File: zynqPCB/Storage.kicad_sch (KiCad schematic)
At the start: 22 parts, among them J3 Micro_SD_Card_Det, U16 FTDITypeUART, U17 ABRACON-ASDMB, U18 S25FL256SAGNFI001, U20F1 xc7z020clg484

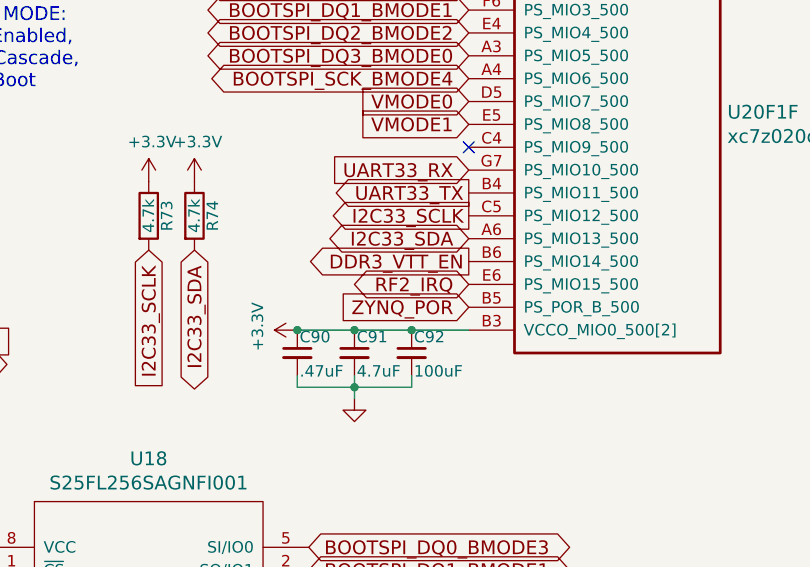
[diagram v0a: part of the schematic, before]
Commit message: Sensores Removed
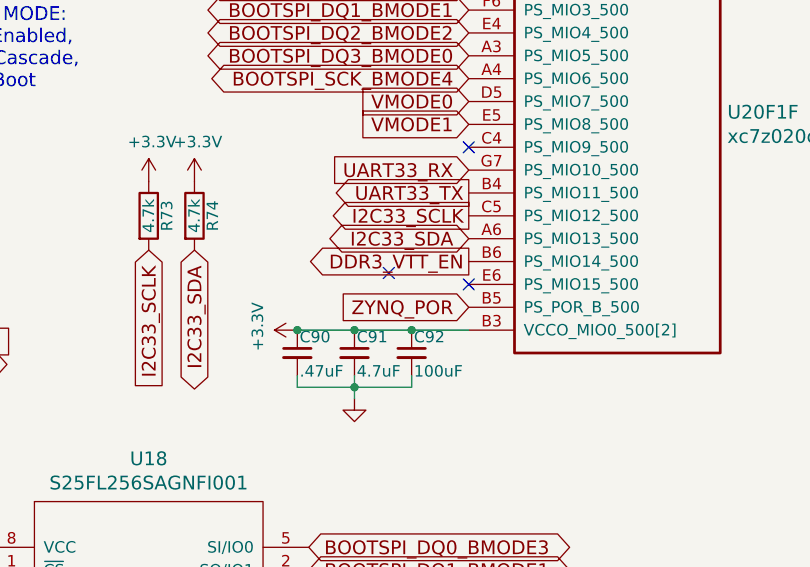
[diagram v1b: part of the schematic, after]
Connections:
- net RF2_IRQ: no longer names the net of U20F1.E6 (PS_MIO15_500)
- no-connect marks 4 -> 6
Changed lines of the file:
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@@
+	)
+	(no_connect
+		(at 198.12 101.6)
 	)
 	(no_connect
@@
 	(no_connect
 		(at 140.97 114.3)
+	)
+	(no_connect
+		(at 207.01 102.87)
 	)
 	(wire
@@
 			(effects
 				(font
-					(size 1.27 1.27)
-				)
-				(hide yes)
-			)
-		)
-	)
-	(global_label "RF2_IRQ"
-		(shape bidirectional)
-		(at 207.01 102.87 180)
-		(effects
-			(font
-				(size 1.524 1.524)
-			)
-			(justify right)
-		)
-		(property "Intersheetrefs" "${INTERSHEET_REFS}"
-			(at 207.01 102.87 0)
-			(effects
-				(font

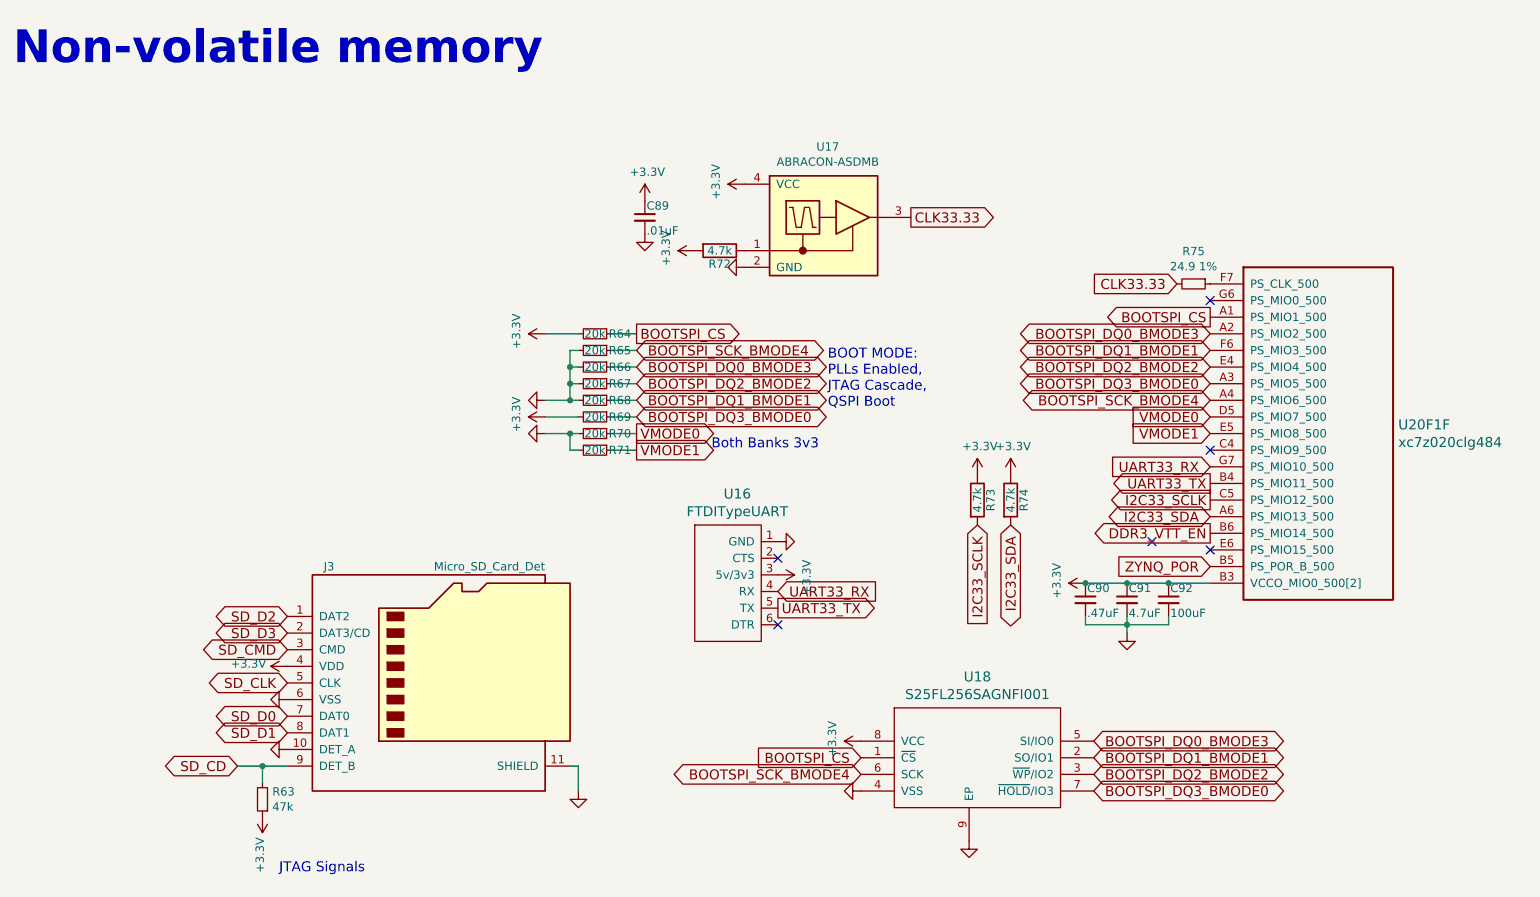
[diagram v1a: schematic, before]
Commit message: sensor changed
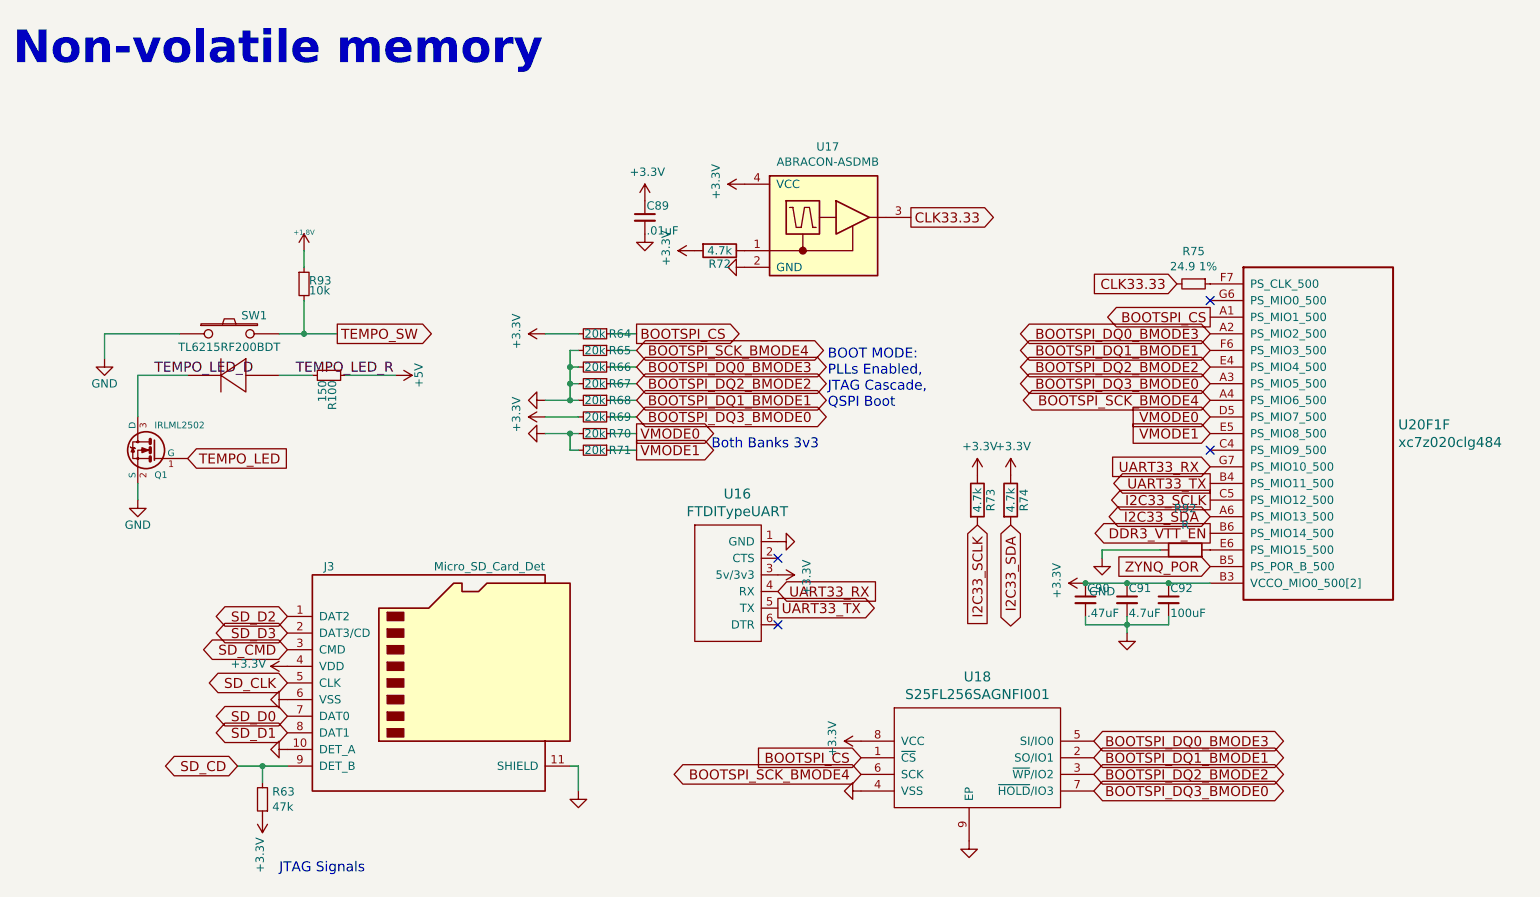
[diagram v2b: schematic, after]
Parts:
- added Q1: IRLML2502, Package_TO_SOT_SMD:SOT-23, symbol DFTBoard-rescue:IRLML2502-
- added R100: 150, Resistor_SMD:R_0402_1005Metric, symbol Device:R_Small
- added R92: R, symbol DFTCustom:R
- added R93: 10k, Resistor_SMD:R_0402_1005Metric, symbol Device:R_Small
- added SW1: TL6215RF200BDT, DFTcustom:tl6215_right_angle, symbol DFTBoard-rescue:SW_IL-
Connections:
- net GND: now also Q1.2 (S), R92.1, SW1.1
- net at U20F1.E6 (PS_MIO15_500): now also R92.2
- new net +1.8V: R93.1
- new net +5V: R100.1
- new net TEMPO_LED: Q1.1 (G)
- new net TEMPO_LED_D: Q1.3 (D), SW1.3
- new net TEMPO_LED_R: R100.2, SW1.4
- new net TEMPO_SW: R93.2, SW1.2
- no-connect marks 6 -> 4
